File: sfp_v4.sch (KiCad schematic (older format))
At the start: 83 parts, among them J101 CONN_COAXIAL, J102 CONN_COAXIAL, J103 CONN_COAXIAL, J104 CONN_COAXIAL, J105 CONN_COAXIAL, J106 CONN_COAXIAL, P101 SFP-CONNECTOR, P103 CONN_01X01, P104 CONN_01X01, P105 CONN_01X01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

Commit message: add missing component values and comments to schematic
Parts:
- C101, C102, C112, C113: value C -> 100n
- J101, J103, J105: value CONN_COAXIAL -> BNC
- J102, J104, J106: value CONN_COAXIAL -> SMA
- L101, L102, L103, L104, L107, L108: value L -> 2u2
- P101: symbol awallin:SFP-CONNECTOR -> sfp_v4-rescue:SFP-CONNECTOR-awallin
- T101, T102: symbol awallin:ADT16-1T -> sfp_v4-rescue:ADT16-1T-awallin
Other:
- note added: "50R Single-Ended"
- note added: "TX input\n-10 dBm to 0 dBm\n1 MHz to 200 MHz"
- note added: "This design is at: https://github.com/aewallin/SFP2SMA_2018.03\nTypical performance: http://www.anderswallin.net/2019/03/sma-to-sfp-frequency-stability/\nnotes: http://www.anderswallin.net/2018/04/500-mhz-sfp-board-v4/\n"
- note added: "option:\nAC-couple with\n100nF cap here?\n"
- note removed: "50R SE"
- note removed: "AC-cpl?"
- note removed: "TX input"
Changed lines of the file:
@@
 EESchema Schematic File Version 4
-EELAYER 26 0
+LIBS:sfp_v4-cache
+EELAYER 29 0
 EELAYER END
 $Descr A4 11693 8268
@@
 RD+
 $Comp
-L awallin:SFP-CONNECTOR P101
+L sfp_v4-rescue:SFP-CONNECTOR-awallin P101
 U 1 1 5620A480
 P 1350 5800
@@
 U 1 1 58C2D783
 P 7600 1800
-F 0 "J102" H 7610 1920 50  0000 C CNN
-F 1 "CONN_COAXIAL" V 7715 1800 50  0000 C CNN
+F 0 "J102" H 7400 1900 50  0000 C CNN
+F 1 "SMA" H 7800 1800 50  0000 C CNN
 F 2 "awallinKiCadFootprints:CONNECTOR_SMA_Straight" H 7600 1800 50  0001 C CNN
 F 3 "" H 7600 1800 50  0001 C CNN
@@
 P 10000 5550
 F 0 "J104" H 10010 5670 50  0000 C CNN
-F 1 "CONN_COAXIAL" V 10115 5550 50  0000 C CNN
+F 1 "SMA" H 10150 5550 50  0000 C CNN
 F 2 "awallinKiCadFootprints:CONNECTOR_SMA_Straight" H 10000 5550 50  0001 C CNN
 F 3 "" H 10000 5550 50  0001 C CNN
@@
 P 7600 1250
 F 0 "J101" H 7610 1370 50  0000 C CNN
-F 1 "CONN_COAXIAL" V 7715 1250 50  0000 C CNN
+F 1 "BNC" H 7800 1250 50  0000 C CNN
 F 2 "awallinKiCadFootprints:BNC_2PIN" H 7600 1250 50  0001 C CNN
 F 3 "" H 7600 1250 50  0001 C CNN
@@
 	1    0    0    -1
 $EndComp
-Text Notes 10250 5550 0    60   ~ 0
-TX input
+Text Notes 10200 5400 0    60   ~ 0
+TX input\n-10 dBm to 0 dBm\n1 MHz to 200 MHz
 $Comp
 L sfp_v4-rescue:Conn_Coaxial J103
@@
 P 10000 4900
 F 0 "J103" H 10010 5020 50  0000 C CNN
-F 1 "CONN_COAXIAL" V 10115 4900 50  0000 C CNN
+F 1 "BNC" H 10150 4900 50  0000 C CNN
 F 2 "awallinKiCadFootprints:BNC_2PIN" H 10000 4900 50  0001 C CNN
 F 3 "" H 10000 4900 50  0001 C CNN
@@
 P 6500 2300
 F 0 "L102" V 6450 2300 50  0000 C CNN
-F 1 "L" V 6575 2300 50  0000 C CNN
+F 1 "2u2" V 6575 2300 50  0000 C CNN
 F 2 "Resistors_SMD:R_0805" H 6500 2300 50  0001 C CNN
 F 3 "" H 6500 2300 50  0001 C CNN
@@
 P 6500 1250
 F 0 "L101" V 6450 1250 50  0000 C CNN
-F 1 "L" V 6575 1250 50  0000 C CNN
+F 1 "2u2" V 6575 1250 50  0000 C CNN
 F 2 "Resistors_SMD:R_0805" H 6500 1250 50  0001 C CNN
 F 3 "" H 6500 1250 50  0001 C CNN
@@
 P 9300 3550
 F 0 "L104" V 9250 3550 50  0000 C CNN
-F 1 "L" V 9375 3550 50  0000 C CNN
+F 1 "2u2" V 9375 3550 50  0000 C CNN
 F 2 "Resistors_SMD:R_0805" H 9300 3550 50  0001 C CNN
 F 3 "" H 9300 3550 50  0001 C CNN
@@
 P 9300 2500
 F 0 "L103" V 9250 2500 50  0000 C CNN
-F 1 "L" V 9375 2500 50  0000 C CNN
+F 1 "2u2" V 9375 2500 50  0000 C CNN
 F 2 "Resistors_SMD:R_0805" H 9300 2500 50  0001 C CNN
 F 3 "" H 9300 2500 50  0001 C CNN
@@
 P 2150 2700
 F 0 "C112" H 2175 2800 50  0000 L CNN
-F 1 "C" H 2175 2600 50  0000 L CNN
+F 1 "100n" H 2175 2600 50  0000 L CNN
 F 2 "Capacitors_SMD:C_0805" H 2188 2550 50  0001 C CNN
 F 3 "" H 2150 2700 50  0001 C CNN
@@
 P 2150 3200
 F 0 "C113" H 2175 3300 50  0000 L CNN
-F 1 "C" H 2175 3100 50  0000 L CNN
+F 1 "100n" H 2175 3100 50  0000 L CNN
 F 2 "Capacitors_SMD:C_0805" H 2188 3050 50  0001 C CNN
 F 3 "" H 2150 3200 50  0001 C CNN
@@
 $EndComp
 $Comp
-L awallin:ADT16-1T T102
+L sfp_v4-rescue:ADT16-1T-awallin T102
 U 1 1 58D28ACC
 P 3200 2950
@@
 $EndComp
 Text Notes 3600 2700 0    60   ~ 0
-50R SE
+50R Single-Ended
 Text Notes 2350 2600 0    60   ~ 0
 100R DIFF
 $Comp
-L awallin:ADT16-1T T101
+L sfp_v4-rescue:ADT16-1T-awallin T101
 U 1 1 58D2D49B
 P 3450 1900
@@
 P 2200 1750
 F 0 "C101" H 2225 1850 50  0000 L CNN
-F 1 "C" H 2225 1650 50  0000 L CNN
+F 1 "100n" H 2225 1650 50  0000 L CNN
 F 2 "Capacitors_SMD:C_0805" H 2238 1600 50  0001 C CNN
 F 3 "" H 2200 1750 50  0001 C CNN
@@
 P 2200 2050
 F 0 "C102" H 2225 2150 50  0000 L CNN
-F 1 "C" H 2225 1950 50  0000 L CNN
+F 1 "100n" H 2225 1950 50  0000 L CNN
 F 2 "Capacitors_SMD:C_0805" H 2238 1900 50  0001 C CNN
 F 3 "" H 2200 2050 50  0001 C CNN
@@
 100R DIFF
 Text Notes 3650 1600 0    60   ~ 0
-50R SE
+50R Single-Ended
 Text Notes 10650 2750 0    60   ~ 0
 RX output2
@@
 P 10400 2500
 F 0 "J105" H 10410 2620 50  0000 C CNN
-F 1 "CONN_COAXIAL" V 10515 2500 50  0000 C CNN
+F 1 "BNC" H 10600 2500 50  0000 C CNN
 F 2 "awallinKiCadFootprints:BNC_2PIN" H 10400 2500 50  0001 C CNN
 F 3 "" H 10400 2500 50  0001 C CNN
@@
 U 1 1 58C4374B
 P 10400 3050
-F 0 "J106" H 10410 3170 50  0000 C CNN
-F 1 "CONN_COAXIAL" V 10515 3050 50  0000 C CNN
+F 0 "J106" H 10250 3150 50  0000 C CNN
+F 1 "SMA" H 10600 3050 50  0000 C CNN
 F 2 "awallinKiCadFootprints:CONNECTOR_SMA_Straight" H 10400 3050 50  0001 C CNN
 F 3 "" H 10400 3050 50  0001 C CNN
@@
 P 7500 5800
 F 0 "L107" V 7450 5800 50  0000 C CNN
-F 1 "L" V 7575 5800 50  0000 C CNN
+F 1 "2u2" V 7575 5800 50  0000 C CNN
 F 2 "Resistors_SMD:R_0805" H 7500 5800 50  0001 C CNN
 F 3 "" H 7500 5800 50  0001 C CNN
@@
 Wire Wire Line
 	6050 4900 6300 4900
-Text Notes 5750 4750 0    60   ~ 0
-AC-cpl?
+Text Notes 5450 4700 0    60   ~ 0
+option:\nAC-couple with\n100nF cap here?\n
 Wire Wire Line
 	6300 5350 7300 5350
@@
 P 7750 4400
 F 0 "L108" V 7700 4400 50  0000 C CNN
-F 1 "L" V 7825 4400 50  0000 C CNN
+F 1 "2u2" V 7825 4400 50  0000 C CNN
 F 2 "Resistors_SMD:R_0805" H 7750 4400 50  0001 C CNN
 F 3 "" H 7750 4400 50  0001 C CNN
@@
 NoConn ~ 6900 5200
 NoConn ~ 6800 5200
+Text Notes 700  900  0    60   ~ 0
+This design is at: https://github.com/aewallin/SFP2SMA_2018.03\nTypical performance: http://www.anderswallin.net/2019/03/sma-to-sfp-frequency-stability/\nnotes: http://www.anderswallin.net/2018/04/500-mhz-sfp-board-v4/\n
 $EndSCHEMATC

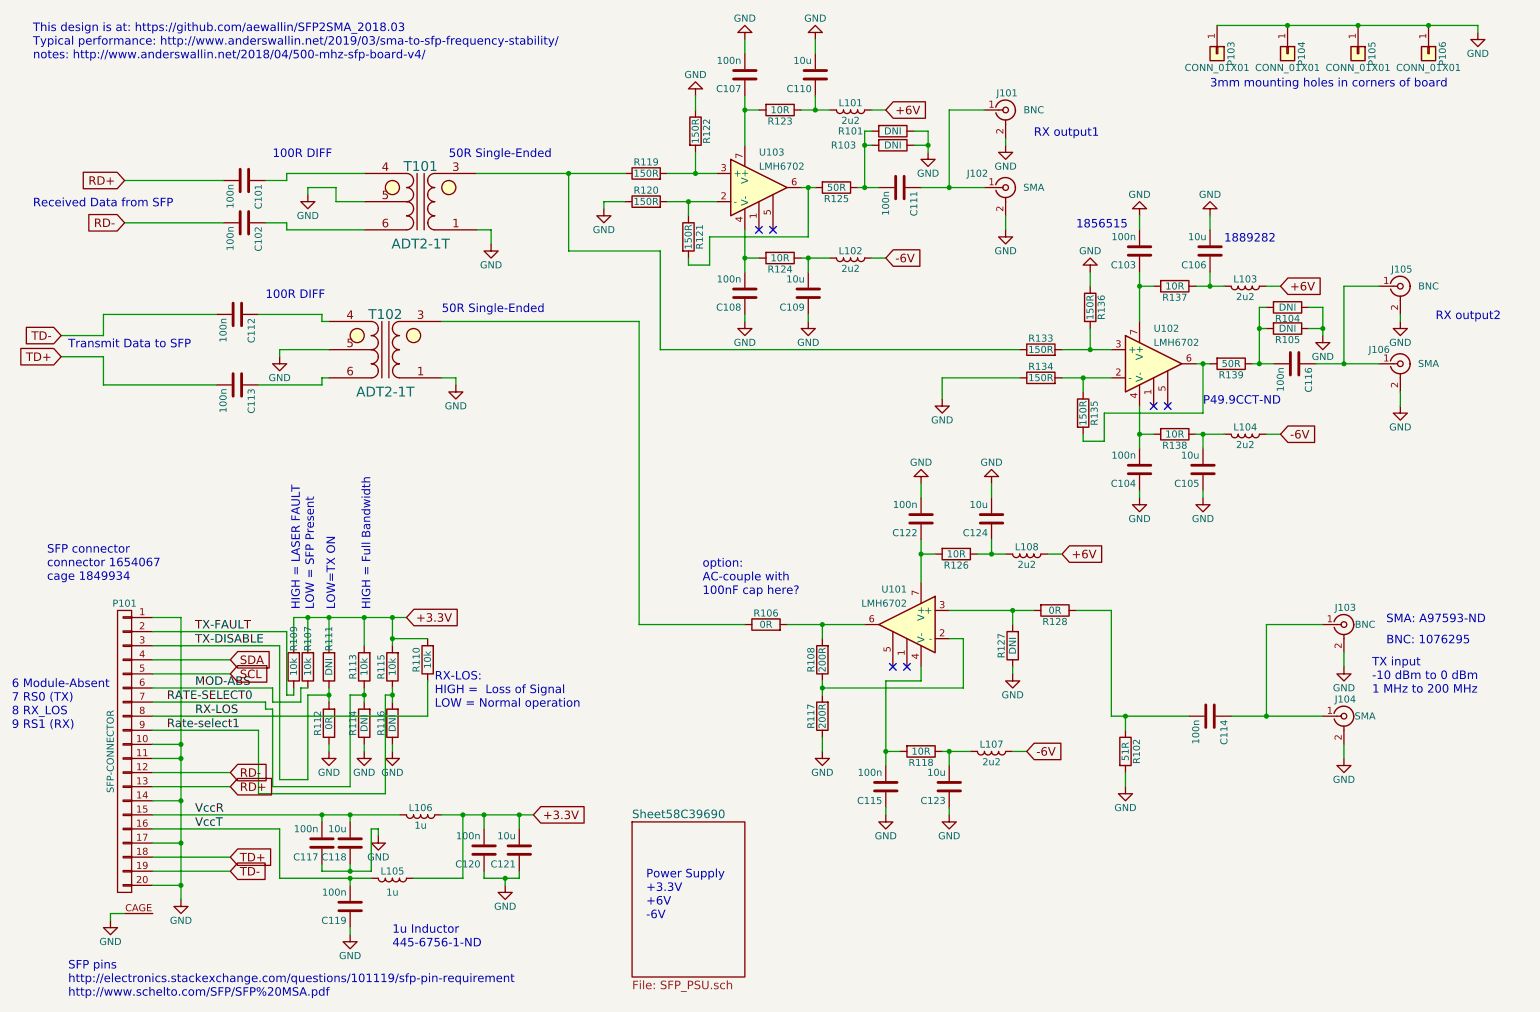
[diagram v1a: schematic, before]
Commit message: revise: kicad standard lib symbols/footprints, add SFP status LEDs
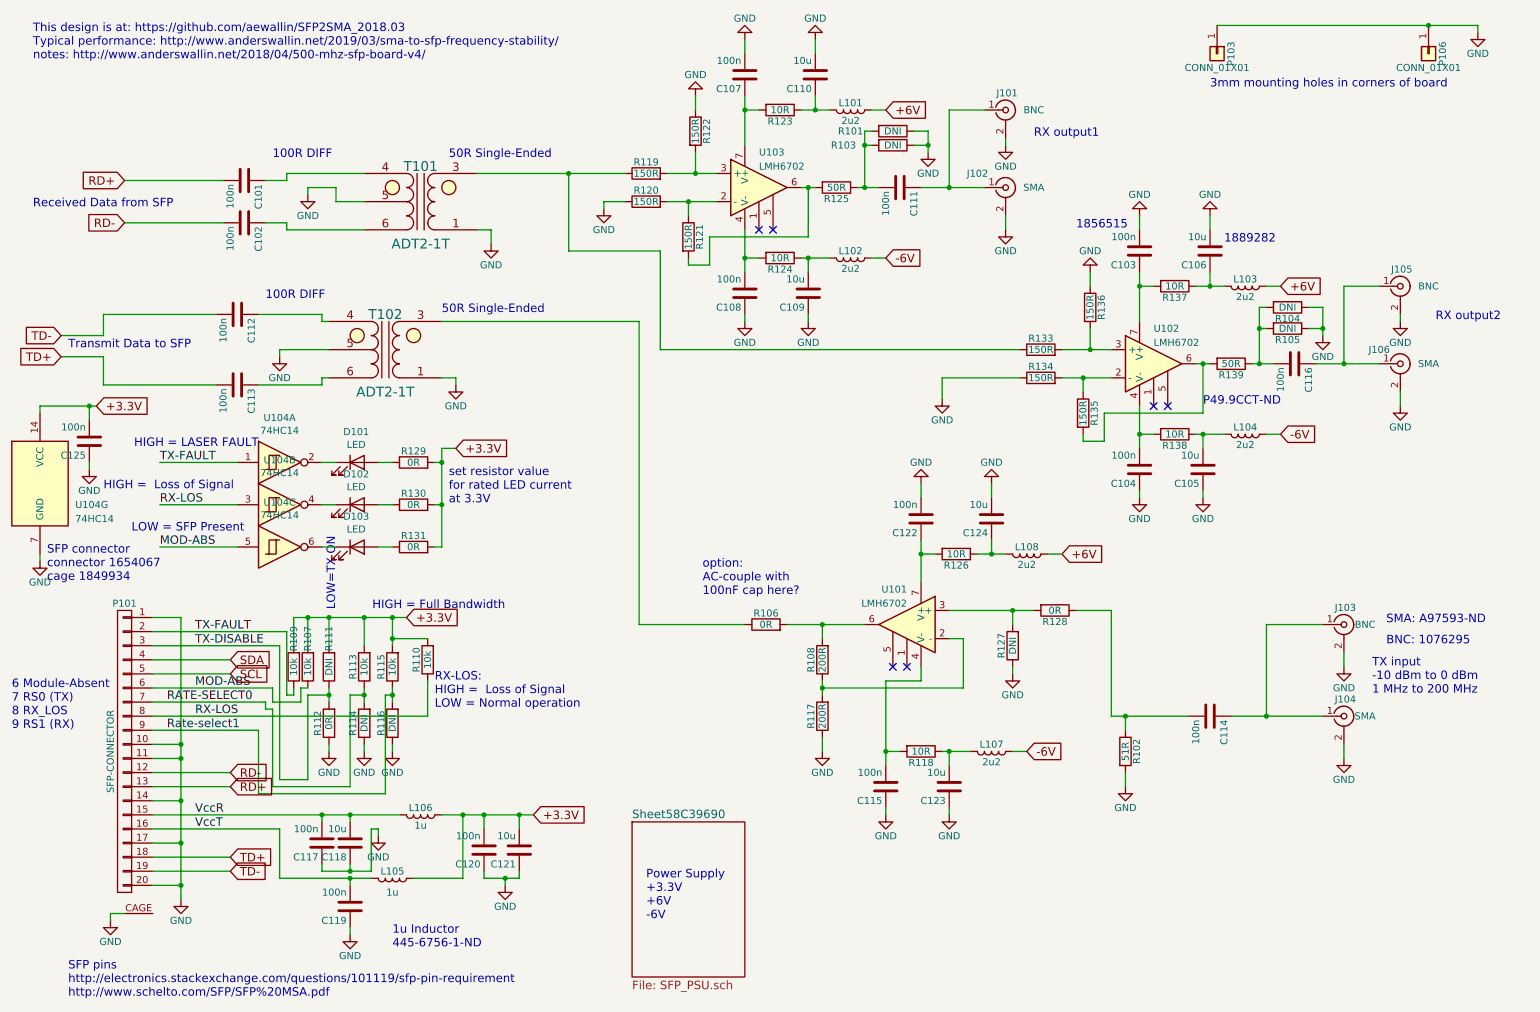
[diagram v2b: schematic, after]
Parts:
- removed P104, P105: CONN_01X01, Mounting_Holes:MountingHole_3mm, symbol sfp_v4-rescue:Conn_01x01
- added C125: 100n, Capacitor_SMD:C_0805_2012Metric, symbol sfp_v4-rescue:C
- added D101, D102, D103: LED, LED_SMD:LED_0805_2012Metric, symbol Device:LED
- added R129, R130, R131: 0R, Resistor_SMD:R_0805_2012Metric, symbol sfp_v4-rescue:R
- added U104: 74HC14, Package_SO:TSSOP-14_4.4x5mm_P0.65mm, symbol 74xx:74HC14
- J102, J104, J106: footprint awallinKiCadFootprints:CONNECTOR_SMA_Straight -> Connector_Coaxial:SMA_Molex_73251-2200_Horizontal
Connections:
- net +3.3V: now also C125.2, R129.2, R130.2, R131.2, U104.14 (VCC)
- net GND: now also C125.1, U104.7 (GND)
- net MOD-ABS: now also U104.5
- net RX-LOS: now also U104.3
- net TX-FAULT: now also U104.1
- new net: D101.1 (K), U104.2
- new net: D102.1 (K), U104.4
- new net: D103.1 (K), U104.6
- new net: D101.2 (A), R129.1
- new net: D102.2 (A), R130.1
- new net: D103.2 (A), R131.1
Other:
- note added: "HIGH = Loss of Signal \n"
- note added: "set resistor value\nfor rated LED current\nat 3.3V"

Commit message: simplify
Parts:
- removed R101, R103, R104, R105, R111, R114, R116, R127: DNI, Resistors_SMD:R_0805, symbol sfp_v4-rescue:R
- removed R106, R112, R128: 0R, Resistors_SMD:R_0805, symbol sfp_v4-rescue:R
- R129, R130, R131: value 0R -> 200R
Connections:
- net TX-DISABLE is gone; now on net GND: P101.3 (P3)
- net at C114.2, R102.1: now also U101.3 (+)
- net at T102.3 (PR_DOT): now also R108.2, U101.6
- net RATE-SELECT0 renamed RS0
- net Rate-select1 renamed RS1
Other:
- note added: "RS0, RS1\nHIGH = \nFull Bandwidth"
- note removed: "HIGH = Full Bandwidth"
- note removed: "RX-LOS:\nHIGH = Loss of Signal \nLOW = Normal operation"
- note removed: "option:\nAC-couple with\n100nF cap here?\n"
- moved on the sheet: R107, R109, R110, R113, R115

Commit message: revise
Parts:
- removed J101, J103, J105: BNC, awallinKiCadFootprints:BNC_2PIN, symbol sfp_v4-rescue:Conn_Coaxial
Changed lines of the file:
@@
 	1    0    0    -1
 $EndComp
-Text Notes 7800 1450 0    60   ~ 0
+Text Notes 7400 1600 0    60   ~ 0
 RX output1
 $Comp
@@
 Text Label 1850 4950 0    60   ~ 0
 TX-FAULT
-$Comp
-L sfp_v4-rescue:Conn_Coaxial J101
-U 1 1 58C387EA
-P 7600 1250
-F 0 "J101" H 7610 1370 50  0000 C CNN
-F 1 "BNC" H 7800 1250 50  0000 C CNN
-F 2 "awallinKiCadFootprints:BNC_2PIN" H 7600 1250 50  0001 C CNN
-F 3 "" H 7600 1250 50  0001 C CNN
-	1    7600 1250
-	1    0    0    -1
-$EndComp
-$Comp
-L sfp_v4-rescue:GND-power #PWR08
-U 1 1 58C38887
-P 7600 1500
-F 0 "#PWR08" H 7600 1250 50  0001 C CNN
-F 1 "GND" H 7600 1350 50  0000 C CNN
-F 2 "" H 7600 1500 60  0000 C CNN
-F 3 "" H 7600 1500 60  0000 C CNN
-	1    7600 1500
-	1    0    0    -1
-$EndComp
 Text Notes 10200 5400 0    60   ~ 0
 TX input\n-10 dBm to 0 dBm\n1 MHz to 200 MHz
-$Comp
-L sfp_v4-rescue:Conn_Coaxial J103
-U 1 1 58C3A125
-P 10000 4900
-F 0 "J103" H 10010 5020 50  0000 C CNN
-F 1 "BNC" H 10150 4900 50  0000 C CNN
-F 2 "awallinKiCadFootprints:BNC_2PIN" H 10000 4900 50  0001 C CNN
-F 3 "" H 10000 4900 50  0001 C CNN
-	1    10000 4900
-	1    0    0    -1
-$EndComp
 $Comp
 L sfp_v4-rescue:GND-power #PWR09
@@
 F 3 "" H 10000 5850 60  0000 C CNN
 	1    10000 5850
-	1    0    0    -1
-$EndComp
-$Comp
-L sfp_v4-rescue:GND-power #PWR010
-U 1 1 58C3A27E
-P 10000 5200
-F 0 "#PWR010" H 10000 4950 50  0001 C CNN
-F 1 "GND" H 10000 5050 50  0000 C CNN
-F 2 "" H 10000 5200 60  0000 C CNN
-F 3 "" H 10000 5200 60  0000 C CNN
-	1    10000 5200
 	1    0    0    -1
 $EndComp
@@
 	1    9650 3050
 	0    1    1    0
-$EndComp
-$Comp
-L sfp_v4-rescue:GND-power #PWR018
-U 1 1 58C43757
-P 10400 2750
-F 0 "#PWR018" H 10400 2500 50  0001 C CNN
-F 1 "GND" H 10400 2600 50  0000 C CNN
-F 2 "" H 10400 2750 60  0000 C CNN
-F 3 "" H 10400 2750 60  0000 C CNN
-	1    10400 2750
-	1    0    0    -1
 $EndComp
 $Comp
@@
 RX output2
 $Comp
-L sfp_v4-rescue:Conn_Coaxial J105
-U 1 1 58C43751
-P 10400 2500
-F 0 "J105" H 10410 2620 50  0000 C CNN
-F 1 "BNC" H 10600 2500 50  0000 C CNN
-F 2 "awallinKiCadFootprints:BNC_2PIN" H 10400 2500 50  0001 C CNN
-F 3 "" H 10400 2500 50  0001 C CNN
-	1    10400 2500
-	1    0    0    -1
-$EndComp
-$Comp
 L sfp_v4-rescue:Conn_Coaxial J106
 U 1 1 58C4374B
@@
 	10950 650  10950 700
 Wire Wire Line
-	7600 1500 7600 1450
-Wire Wire Line
-	7450 1250 7200 1250
-Wire Wire Line
-	7200 1250 7200 1800
-Connection ~ 7200 1800
-Wire Wire Line
-	10000 5200 10000 5100
-Wire Wire Line
 	10000 5850 10000 5750
-Wire Wire Line
-	9850 4900 9450 4900
-Wire Wire Line
-	9450 4900 9450 5550
-Connection ~ 9450 5550
 Wire Wire Line
 	3250 5800 3250 5750
@@
 Connection ~ 5400 1700
 Wire Wire Line
-	7000 1800 7200 1800
-Wire Wire Line
 	6250 1800 6200 1800
 Wire Wire Line
@@
 	10400 3350 10400 3250
 Wire Wire Line
-	10400 2750 10400 2700
-Wire Wire Line
-	10250 2500 10000 2500
-Wire Wire Line
-	10000 2500 10000 3050
-Connection ~ 10000 3050
-Wire Wire Line
 	8350 3150 8150 3150
 Wire Wire Line
@@
 	8200 2800 8200 2950
 Connection ~ 8200 2950
-Wire Wire Line
-	9800 3050 10000 3050
 Wire Wire Line
 	9050 3050 9000 3050
@@
 	2450 6350 2450 6700
 Connection ~ 2950 6700
-Wire Wire Line
-	9200 5550 9450 5550
 Wire Wire Line
 	900  3000 1200 3000
@@
 	1750 5750 1750 5850
 Wire Wire Line
-	7200 1800 7450 1800
-Wire Wire Line
-	9450 5550 9850 5550
-Wire Wire Line
 	5350 1900 5200 1900
 Wire Wire Line
@@
 Wire Wire Line
 	6200 1800 6150 1800
-Wire Wire Line
-	10000 3050 10250 3050
 Wire Wire Line
 	8150 3150 8000 3150
@@
 Wire Wire Line
 	6550 1800 6700 1800
+Wire Wire Line
+	9200 5550 9850 5550
+Wire Wire Line
+	9800 3050 10250 3050
+Wire Wire Line
+	7000 1800 7450 1800
 $EndSCHEMATC

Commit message: tune component values
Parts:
- R102: value 51R -> 49R9
- R125, R139: value 50R -> 49R9
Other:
- note added: "Rate Select\nRS0, RS1\nHIGH = \nFull Bandwidth"
- note removed: "RS0, RS1\nHIGH = \nFull Bandwidth"
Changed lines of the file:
@@
 P 6400 1800
 F 0 "R125" V 6480 1800 50  0000 C CNN
-F 1 "50R" V 6400 1800 50  0000 C CNN
+F 1 "49R9" V 6400 1800 50  0000 C CNN
 F 2 "Resistors_SMD:R_0805" V 6330 1800 30  0001 C CNN
 F 3 "" H 6400 1800 30  0000 C CNN
@@
 P 9200 3050
 F 0 "R139" V 9280 3050 50  0000 C CNN
-F 1 "50R" V 9200 3050 50  0000 C CNN
+F 1 "49R9" V 9200 3050 50  0000 C CNN
 F 2 "Resistors_SMD:R_0805" V 9130 3050 30  0001 C CNN
 F 3 "" H 9200 3050 30  0000 C CNN
@@
 $EndComp
 Text Notes 4150 4700 0    60   ~ 0
-RS0, RS1\nHIGH = \nFull Bandwidth
+Rate Select\nRS0, RS1\nHIGH = \nFull Bandwidth
 $Comp
 L sfp_v4-rescue:C C120
@@
 P 8450 5800
 F 0 "R102" V 8530 5800 50  0000 C CNN
-F 1 "51R" V 8450 5800 50  0000 C CNN
+F 1 "49R9" V 8450 5800 50  0000 C CNN
 F 2 "Resistors_SMD:R_0805" V 8380 5800 50  0001 C CNN
 F 3 "" H 8450 5800 50  0001 C CNN

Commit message: minor tuning
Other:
- note added: "Copyright Anders E, Wallin 2020.\nThis source describes Open Hardware and is licensed under the CERN-OHL-P v2\n\nYou may redistribute and modify this documentation and make products\nusing it under the terms of the CERN-OHL-P v2 (https:/cern.ch/cern-ohl).\n\nThis design is at: https://github.com/aewallin/SFP2SMA_2018.03\nTypical performance: http://www.anderswallin.net/2019/03/sma-to-sfp-frequenc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"
- note removed: "This design is at: https://github.com/aewallin/SFP2SMA_2018.03\nTypical performance: http://www.anderswallin.net/2019/03/sma-to-sfp-frequency-stability/\nnotes: http://www.anderswallin.net/2018/04/500-mhz-sfp-board-v4/\n"
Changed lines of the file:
@@
 NoConn ~ 6900 5200
 NoConn ~ 6800 5200
-Text Notes 700  900  0    60   ~ 0
-This design is at: https://github.com/aewallin/SFP2SMA_2018.03\nTypical performance: http://www.anderswallin.net/2019/03/sma-to-sfp-frequency-stability/\nnotes: http://www.anderswallin.net/2018/04/500-mhz-sfp-board-v4/\n
+Text Notes 650  1450 0    60   ~ 0
+Copyright Anders E, Wallin 2020.\nThis source describes Open Hardware and is licensed under the CERN-OHL-P v2\n\nYou may redistribute and modify this documentation and make products\nusing it under the terms of the CERN-OHL-P v2 (https:/cern.ch/cern-ohl).\n\nThis design is at: https://github.com/aewallin/SFP2SMA_2018.03\nTypical performance: http://www.anderswallin.net/2019/03/sma-to-sfp-frequency-stability/\nnotes: http://www.anderswallin.net/2018/04/500-mhz-sfp-board-v4/\n
 $Comp
 L 74xx:74HC14 U104
